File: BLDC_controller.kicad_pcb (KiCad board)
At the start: 4 copper layers, 100 x 100 mm, 1554 parts, among them P2 CONN_01X06, P3 CONN_01X05, P5 CONN_01X05, Q1 PSMN2R0-30YLD, Q2 PSMN2R0-30YLD, Q3 PSMN2R0-30YLD, Q4 PSMN2R0-30YLD, Q5 PSMN2R0-30YLD, Q6 PSMN2R0-30YLD

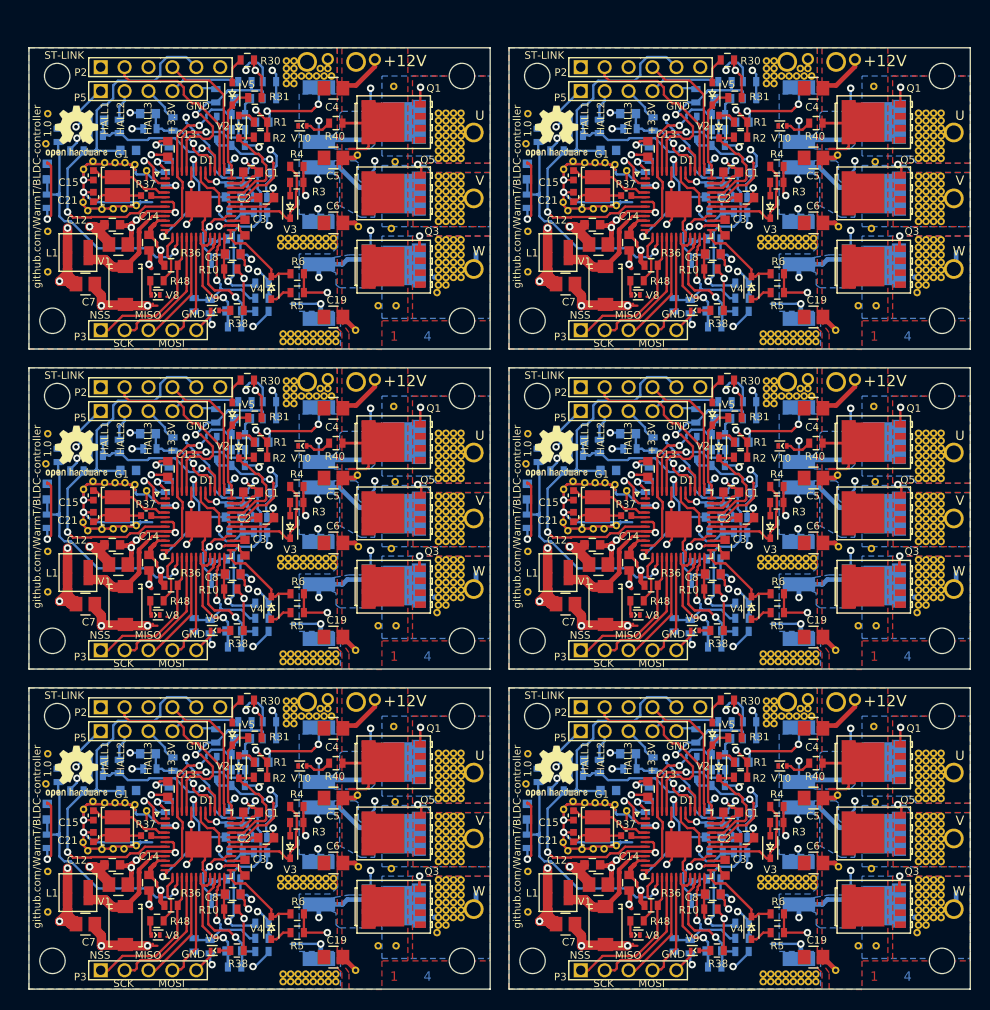
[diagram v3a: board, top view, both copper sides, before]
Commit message: QFN package improved
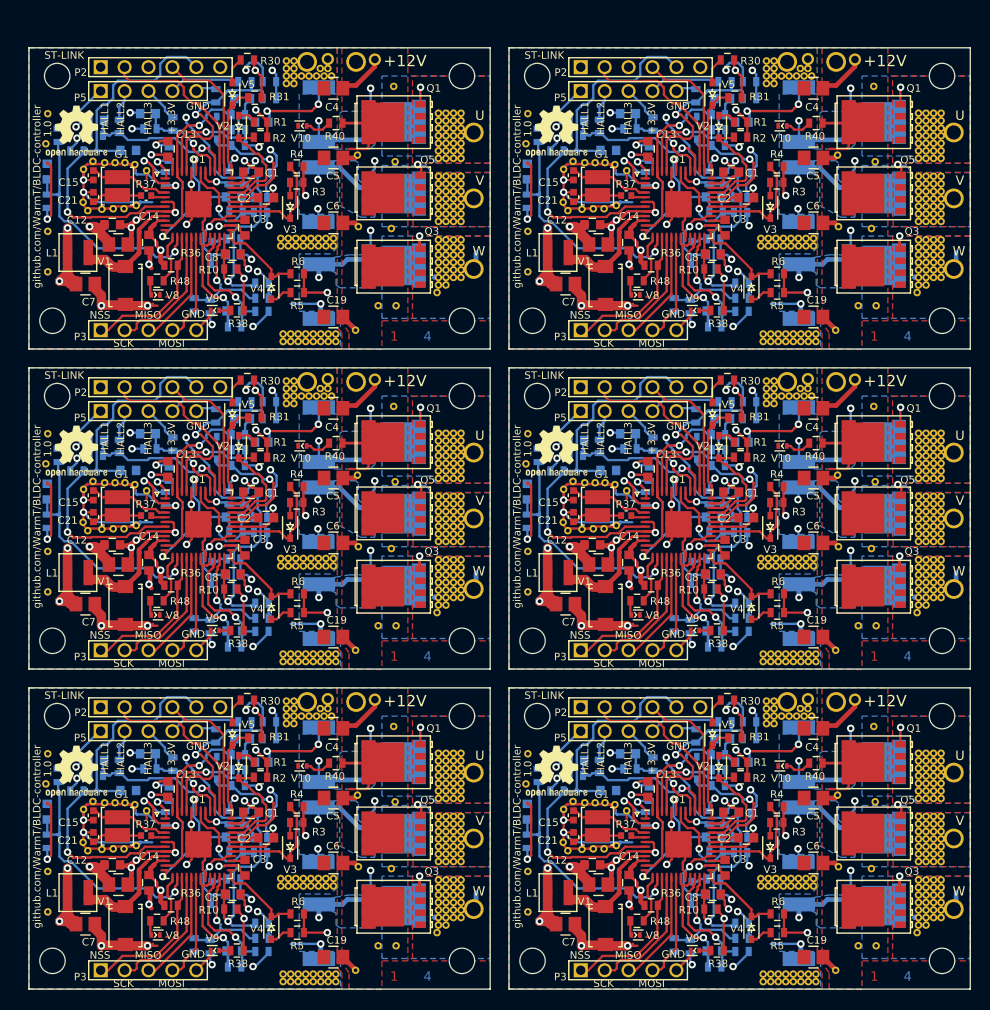
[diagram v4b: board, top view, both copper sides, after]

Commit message: Add Helsinki Hacklab logo
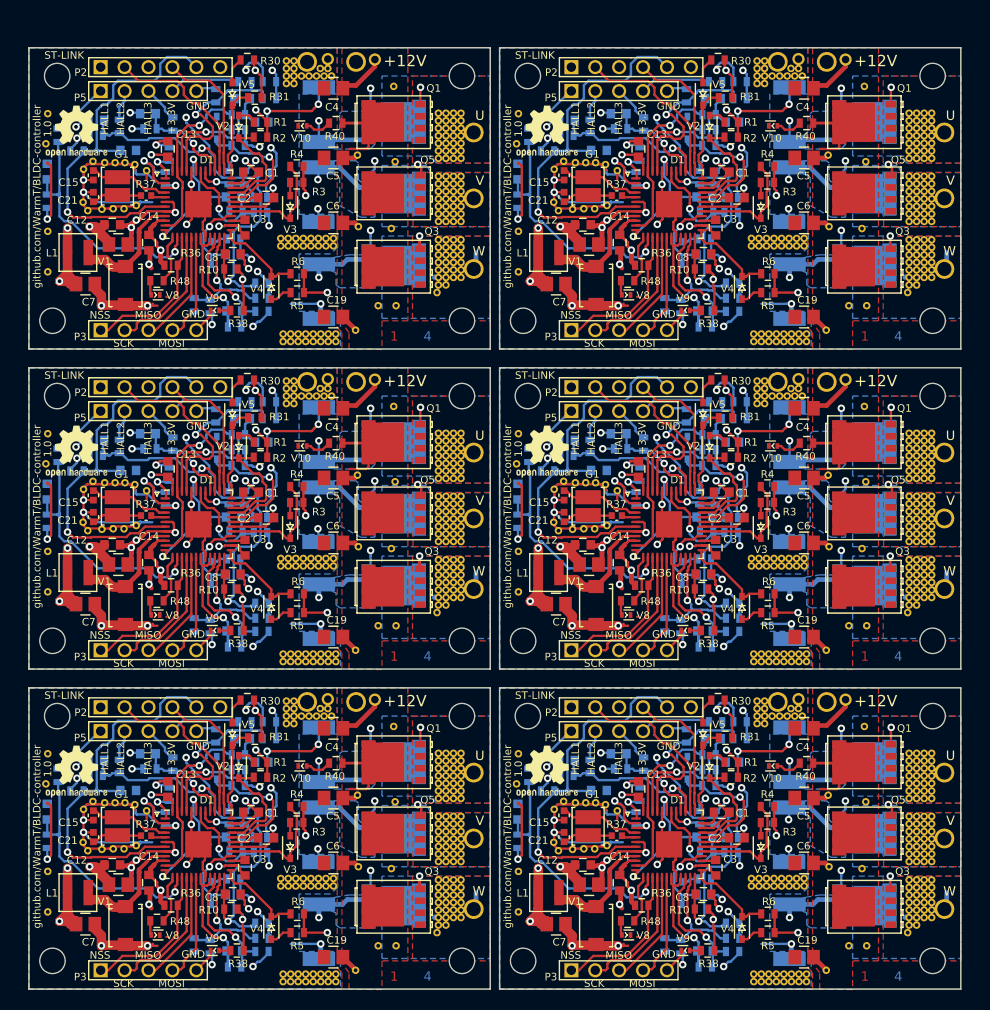
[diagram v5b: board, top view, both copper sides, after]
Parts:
- removed the C1 at (210.8, 162.2)
- removed the C1 at (210.8, 128.2)
- removed the C1 at (210.8, 94.2)
- removed the C10 at (209.0, 164.8)
- removed the C10 at (209.0, 130.8)
- removed the C10 at (209.0, 96.8)
- removed the C11 at (209.9, 154.4)
- removed the C11 at (209.9, 120.4)
- removed the C11 at (209.9, 86.4)
- removed the C12 at (196.1, 167.8)
- removed the C12 at (196.1, 133.8)
- removed the C12 at (196.1, 99.8)
- removed the C13 at (202.0, 159.8)
- removed the C13 at (202.0, 125.8)
- removed the C13 at (202.0, 91.8)
- removed the C14 at (200.0, 169.7)
- removed the C14 at (200.0, 135.7)
- removed the C14 at (200.0, 101.7)
- removed the C15 at (194.1, 162.6)
- removed the C15 at (194.1, 128.6)
- removed the C15 at (194.1, 94.5)
- removed the C16 at (197.8, 159.9)
- removed the C16 at (197.8, 125.9)
- removed the C16 at (197.8, 91.9)
- removed the C17 at (196.8, 169.9)
- removed the C17 at (196.8, 135.9)
- removed the C17 at (196.8, 101.9)
- removed the C19 at (219.6, 177.6)
- removed the C19 at (219.6, 143.6)
- removed the C19 at (219.6, 109.6)
- removed the C2 at (212.4, 164.9)
- removed the C2 at (212.4, 130.9)
- removed the C2 at (212.4, 96.9)
- removed the C21 at (194.1, 164.8)
- removed the C21 at (194.1, 130.8)
- removed the C21 at (194.1, 96.8)
- removed the C22 at (189.2, 162.2)
- removed the C22 at (189.2, 128.2)
- removed the C22 at (189.2, 94.2)
- removed the C23 at (194.4, 156.7)
- removed the C23 at (194.4, 122.7)
- removed the C23 at (194.4, 88.7)
- removed the C24 at (199.9, 156.0)
- removed the C24 at (199.9, 122.0)
- removed the C24 at (199.9, 88.0)
- removed the C3 at (210.2, 168.1)
- removed the C3 at (210.2, 134.1)
- removed the C3 at (210.2, 100.1)
- removed the C4 at (219.6, 153.3)
- removed the C4 at (219.6, 119.3)
- removed the C4 at (219.6, 85.3)
- removed the C5 at (219.6, 160.7)
- removed the C5 at (219.6, 126.7)
- removed the C5 at (219.6, 92.7)
- removed the C6 at (219.6, 167.6)
- removed the C6 at (219.6, 133.6)
- removed the C6 at (219.6, 99.6)
- removed the C7 at (193.2, 174.1)
- removed the C7 at (193.2, 140.1)
- removed the C7 at (193.2, 106.1)
- removed the C8 at (208.9, 170.9)
- removed the C8 at (208.9, 136.9)
- removed the C8 at (208.9, 102.9)
- removed the C9 at (209.1, 176.9)
- removed the C9 at (209.1, 142.9)
- removed the C9 at (209.1, 109.0)
- removed the D1 at (205.2, 165.6)
- removed the D1 at (205.2, 131.6)
- removed the D1 at (205.2, 97.6)
- removed the G1 at (196.7, 163.7)
- removed the G1 at (196.7, 129.7)
- removed the G1 at (196.7, 95.7)
- removed the L1 at (192.4, 170.8)
- removed the L1 at (192.4, 136.8)
- removed the L1 at (192.4, 102.8)
- removed the P2 at (201.2, 151.1)
- removed the P2 at (201.2, 117.1)
- removed the P2 at (201.2, 83.1)
- removed the P3 at (199.9, 179.0)
- removed the P3 at (199.9, 145.0)
- removed the P3 at (199.9, 111.0)
- removed the P5 at (199.9, 153.6)
- removed the P5 at (199.9, 119.6)
- removed the P5 at (199.9, 85.6)
- removed the Q1 at (226.0, 156.9)
- removed the Q1 at (226.0, 122.9)
- removed the Q1 at (226.0, 88.9)
- removed the Q2 at (226.0, 156.9)
- removed the Q2 at (226.0, 122.9)
- removed the Q2 at (226.0, 88.9)
- removed the Q3 at (226.0, 172.3)
- removed the Q3 at (226.0, 138.3)
- removed the Q3 at (226.0, 104.3)
- removed the Q4 at (226.0, 172.1)
- removed the Q4 at (226.0, 138.1)
- removed the Q4 at (226.0, 104.1)
- removed the Q5 at (226.0, 164.5)
- removed the Q5 at (226.0, 130.5)
- removed the Q5 at (226.0, 96.5)
- removed the Q6 at (226.0, 164.5)
- removed the Q6 at (226.0, 130.5)
- removed the Q6 at (226.0, 96.5)
- removed the R1 at (211.8, 156.9)
- removed the R1 at (211.8, 122.9)
- removed the R1 at (211.8, 88.9)
- removed the R10 at (208.7, 172.5)
- removed the R10 at (208.7, 138.5)
- removed the R10 at (208.7, 104.5)
- removed the R11 at (212.0, 174.0)
- removed the R11 at (212.0, 140.0)
- removed the R11 at (212.0, 106.0)
- removed the R12 at (212.2, 162.3)
- removed the R12 at (212.2, 128.3)
- removed the R12 at (212.2, 94.3)
- removed the R13 at (212.8, 152.6)
- removed the R13 at (212.8, 118.6)
- removed the R13 at (212.8, 84.6)
- removed the R14 at (212.0, 177.0)
- removed the R14 at (212.0, 143.0)
- removed the R14 at (212.0, 109.0)
- removed the R15 at (212.1, 156.9)
- removed the R15 at (212.1, 122.9)
- removed the R15 at (212.1, 88.9)
- removed the R16 at (211.8, 166.5)
- removed the R16 at (211.8, 132.5)
- removed the R16 at (211.8, 98.5)
- removed the R17 at (212.0, 175.6)
- removed the R17 at (212.0, 141.6)
- removed the R17 at (212.0, 107.6)
- removed the R18 at (211.8, 164.9)
- removed the R18 at (211.8, 130.9)
- removed the R18 at (211.8, 96.9)
- removed the R19 at (212.8, 154.4)
- removed the R19 at (212.8, 120.4)
- removed the R19 at (212.8, 86.4)
- removed the R2 at (211.8, 158.5)
- removed the R2 at (211.8, 124.5)
- removed the R2 at (211.8, 90.5)
- removed the R20 at (206.5, 176.5)
- removed the R20 at (206.5, 142.5)
- removed the R20 at (206.5, 108.5)
- removed the R21 at (210.2, 162.8)
- removed the R21 at (210.2, 128.8)
- removed the R21 at (210.2, 94.8)
- removed the R22 at (210.2, 152.6)
- removed the R22 at (210.2, 118.6)
- removed the R22 at (210.2, 84.6)
- removed the R23 at (204.8, 176.3)
- removed the R23 at (204.8, 142.3)
- removed the R23 at (204.8, 108.3)
- removed the R24 at (208.5, 162.8)
- removed the R24 at (208.5, 128.8)
- removed the R24 at (208.5, 94.8)
- removed the R25 at (207.1, 154.1)
- removed the R25 at (207.1, 120.1)
- removed the R25 at (207.1, 86.1)
- removed the R26 at (209.1, 178.7)
- removed the R26 at (209.1, 144.7)
- removed the R26 at (209.1, 110.7)
- removed the R27 at (209.2, 166.4)
- removed the R27 at (209.2, 132.4)
- removed the R27 at (209.2, 98.4)
- removed the R28 at (209.5, 156.1)
- removed the R28 at (209.5, 122.1)
- removed the R28 at (209.5, 88.1)
- removed the R29 at (202.2, 160.3)
- removed the R29 at (202.2, 126.3)
- removed the R29 at (202.2, 92.3)
- removed the R3 at (215.7, 163.3)
- removed the R3 at (215.7, 129.3)
- removed the R3 at (215.7, 95.3)
- removed the R30 at (210.4, 150.3)
- removed the R30 at (210.4, 116.3)
- removed the R30 at (210.4, 82.3)
- removed the R31 at (211.2, 154.3)
- removed the R31 at (211.2, 120.3)
- removed the R31 at (211.2, 86.3)
- removed the R32 at (209.5, 157.7)
- removed the R32 at (209.5, 123.7)
- removed the R32 at (209.5, 89.7)
- removed the R33 at (209.5, 159.4)
- removed the R33 at (209.5, 125.4)
- removed the R33 at (209.5, 91.4)
- removed the R34 at (209.0, 169.3)
- removed the R34 at (209.0, 135.3)
- removed the R34 at (209.0, 101.3)
- removed the R35 at (209.0, 171.0)
- removed the R35 at (209.0, 137.0)
- removed the R35 at (209.0, 103.0)
- removed the R36 at (202.3, 172.1)
- removed the R36 at (202.3, 138.1)
- removed the R36 at (202.3, 104.1)
- removed the R37 at (199.7, 164.7)
- removed the R37 at (199.7, 130.7)
- removed the R37 at (199.7, 96.7)
- removed the R38 at (209.3, 176.9)
- removed the R38 at (209.3, 142.9)
- removed the R38 at (209.3, 108.9)
- removed the R39 at (192.3, 159.9)
- removed the R39 at (192.3, 126.0)
- removed the R39 at (192.3, 92.0)
- removed the R4 at (215.7, 161.6)
- removed the R4 at (215.7, 127.6)
- removed the R4 at (215.7, 93.6)
- removed the R40 at (219.8, 157.0)
- removed the R40 at (219.8, 123.0)
- removed the R40 at (219.8, 89.0)
- removed the R41 at (190.3, 158.3)
- removed the R41 at (190.3, 124.3)
- removed the R41 at (190.3, 90.3)
- removed the R42 at (196.8, 157.3)
- removed the R42 at (196.8, 123.3)
- removed the R42 at (196.8, 89.3)
- removed the R43 at (202.6, 157.1)
- removed the R43 at (202.6, 123.1)
- removed the R43 at (202.6, 89.1)
- removed the R44 at (189.2, 165.3)
- removed the R44 at (189.2, 131.3)
- removed the R44 at (189.2, 97.3)
- removed the R45 at (194.4, 158.3)
- removed the R45 at (194.4, 124.3)
- removed the R45 at (194.4, 90.3)
- removed the R46 at (200.1, 157.6)
- removed the R46 at (200.1, 123.6)
- removed the R46 at (200.1, 89.6)
- removed the R47 at (201.8, 162.9)
- removed the R47 at (201.8, 128.9)
- removed the R47 at (201.8, 94.9)
- removed the R48 at (200.8, 173.8)
- removed the R48 at (200.8, 139.8)
- removed the R48 at (200.8, 105.8)
- removed the R5 at (215.8, 175.0)
- removed the R5 at (215.8, 141.0)
- removed the R5 at (215.8, 107.0)
- removed the R6 at (215.8, 173.0)
- removed the R6 at (215.8, 139.0)
- removed the R6 at (215.8, 105.0)
- removed the R7 at (218.1, 174.9)
- removed the R7 at (218.1, 140.9)
- removed the R7 at (218.1, 106.9)
- removed the R8 at (218.0, 164.6)
- removed the R8 at (218.0, 130.6)
- removed the R8 at (218.0, 96.6)
- removed the R9 at (218.1, 156.1)
- removed the R9 at (218.1, 122.1)
- removed the R9 at (218.1, 88.1)
- removed the REF** at (190.2, 152.0)
- removed the REF** at (189.1, 91.2)
- removed the REF** at (230.8, 103.8)
- removed the REF** at (234.5, 172.5)
- removed the REF** at (234.5, 138.5)
- removed the REF** at (234.5, 104.5)
- removed the REF** at (231.6, 174.2)
- removed the REF** at (231.6, 140.2)
- removed the REF** at (189.2, 156.0)
- removed the REF** at (231.6, 106.2)
- removed the REF** at (233.2, 173.4)
- removed the REF** at (233.2, 139.4)
- removed the REF** at (233.2, 105.4)
- removed the REF** at (231.6, 171.8)
- removed the REF** at (231.6, 137.8)
- removed the REF** at (231.6, 103.8)
- removed the REF** at (232.3, 172.6)
- removed the REF** at (232.3, 138.6)
- removed the REF** at (232.3, 104.6)
- removed the REF** at (232.3, 171.8)
- removed the REF** at (232.3, 137.8)
- removed the REF** at (189.2, 122.0)
- removed the REF** at (232.3, 103.8)
- removed the REF** at (233.2, 172.6)
- removed the REF** at (233.2, 138.6)
- removed the REF** at (233.2, 104.6)
- removed the REF** at (231.6, 172.6)
- removed the REF** at (231.6, 138.6)
- removed the REF** at (231.6, 104.6)
- removed the REF** at (233.2, 171.8)
- removed the REF** at (233.2, 137.8)
- removed the REF** at (233.2, 103.8)
- removed the REF** at (230.8, 173.4)
- removed the REF** at (230.8, 139.4)
- removed the REF** at (189.2, 88.0)
- removed the REF** at (230.8, 105.4)
- removed the REF** at (230.8, 174.2)
- removed the REF** at (230.8, 140.2)
- removed the REF** at (230.8, 106.2)
- removed the REF** at (230.8, 172.6)
- removed the REF** at (230.8, 138.6)
- removed the REF** at (193.5, 166.3)
- removed the REF** at (230.8, 104.6)
- removed the REF** at (230.6, 175.0)
- removed the REF** at (230.6, 141.0)
- removed the REF** at (230.6, 107.0)
- removed the REF** at (230.8, 169.4)
- removed the REF** at (230.8, 135.4)
- removed the REF** at (230.8, 101.4)
- removed the REF** at (230.8, 171.0)
- removed the REF** at (230.8, 137.0)
- removed the REF** at (230.8, 103.0)
- removed the REF** at (231.6, 170.2)
- removed the REF** at (231.6, 136.2)
- removed the REF** at (193.5, 132.3)
- removed the REF** at (231.6, 102.2)
- removed the REF** at (231.6, 171.0)
- removed the REF** at (231.6, 137.0)
- removed the REF** at (231.6, 103.0)
- removed the REF** at (231.6, 169.4)
- removed the REF** at (231.6, 135.4)
- removed the REF** at (231.6, 101.4)
- removed the REF** at (230.8, 170.2)
- removed the REF** at (230.8, 136.2)
- removed the REF** at (230.8, 102.2)
- removed the REF** at (232.3, 169.4)
- removed the REF** at (232.3, 135.4)
- removed the REF** at (193.5, 98.3)
- removed the REF** at (232.3, 101.4)
- removed the REF** at (233.2, 171.0)
- removed the REF** at (233.2, 137.0)
- removed the REF** at (233.2, 103.0)
- removed the REF** at (233.2, 169.4)
- removed the REF** at (233.2, 135.4)
- removed the REF** at (193.1, 161.9)
- removed the REF** at (233.2, 101.4)
- removed the REF** at (232.3, 171.0)
- removed the REF** at (232.3, 137.0)
- removed the REF** at (232.3, 103.0)
- removed the REF** at (232.3, 170.2)
- removed the REF** at (232.3, 136.2)
- removed the REF** at (232.3, 102.2)
- removed the REF** at (233.2, 170.2)
- removed the REF** at (233.2, 136.2)
- removed the REF** at (233.2, 102.2)
- removed the REF** at (232.3, 165.8)
- removed the REF** at (232.3, 131.8)
- removed the REF** at (193.1, 127.9)
- removed the REF** at (232.3, 97.8)
- removed the REF** at (233.2, 167.4)
- removed the REF** at (233.2, 133.4)
- removed the REF** at (233.2, 99.5)
- removed the REF** at (233.2, 166.7)
- removed the REF** at (233.2, 132.7)
- removed the REF** at (233.2, 98.7)
- removed the REF** at (232.3, 166.7)
- removed the REF** at (232.3, 132.7)
- removed the REF** at (232.3, 98.7)
- removed the REF** at (232.3, 167.4)
- removed the REF** at (232.3, 133.4)
- removed the REF** at (193.1, 93.9)
- removed the REF** at (232.3, 99.5)
- removed the REF** at (233.2, 165.8)
- removed the REF** at (233.2, 131.8)
- removed the REF** at (233.2, 97.8)
- removed the REF** at (230.8, 165.8)
- removed the REF** at (230.8, 131.8)
- removed the REF** at (193.0, 165.4)
- removed the REF** at (230.8, 97.8)
- removed the REF** at (231.6, 167.4)
- removed the REF** at (231.6, 133.4)
- removed the REF** at (231.6, 99.5)
- removed the REF** at (230.8, 167.4)
- removed the REF** at (230.8, 133.4)
- removed the REF** at (230.8, 99.5)
- removed the REF** at (231.6, 166.7)
- removed the REF** at (231.6, 132.7)
- removed the REF** at (231.6, 98.7)
- removed the REF** at (230.8, 166.7)
- removed the REF** at (230.8, 132.7)
- removed the REF** at (193.0, 131.4)
- removed the REF** at (230.8, 98.7)
- removed the REF** at (231.6, 165.8)
- removed the REF** at (231.6, 131.8)
- removed the REF** at (231.6, 97.8)
- removed the REF** at (233.2, 157.6)
- removed the REF** at (233.2, 123.5)
- removed the REF** at (233.2, 89.5)
- removed the REF** at (233.2, 156.8)
- removed the REF** at (233.2, 122.8)
- removed the REF** at (233.2, 88.8)
- removed the REF** at (230.8, 155.9)
- removed the REF** at (230.8, 122.0)
- removed the REF** at (190.2, 118.0)
- removed the REF** at (193.0, 97.4)
- removed the REF** at (230.8, 88.0)
- removed the REF** at (230.8, 156.8)
- removed the REF** at (230.8, 122.8)
- removed the REF** at (230.8, 88.8)
- removed the REF** at (231.6, 156.8)
- removed the REF** at (231.6, 122.8)
- removed the REF** at (195.3, 161.2)
- removed the REF** at (231.6, 88.8)
- removed the REF** at (232.3, 156.8)
- removed the REF** at (232.3, 122.8)
- removed the REF** at (232.3, 88.8)
- removed the REF** at (233.2, 152.0)
- removed the REF** at (233.2, 118.0)
- removed the REF** at (233.2, 84.0)
- removed the REF** at (233.2, 155.9)
- removed the REF** at (233.2, 122.0)
- removed the REF** at (233.2, 88.0)
- removed the REF** at (231.6, 155.9)
- removed the REF** at (231.6, 122.0)
- removed the REF** at (195.3, 127.2)
- removed the REF** at (231.6, 88.0)
- removed the REF** at (232.3, 155.9)
- removed the REF** at (232.3, 122.0)
- removed the REF** at (232.3, 88.0)
- removed the REF** at (232.3, 158.3)
- removed the REF** at (232.3, 124.3)
- removed the REF** at (232.3, 90.3)
- removed the REF** at (230.8, 157.6)
- removed the REF** at (230.8, 123.5)
- removed the REF** at (230.8, 89.5)
- removed the REF** at (231.6, 158.3)
- removed the REF** at (231.6, 124.3)
- removed the REF** at (195.3, 93.2)
- removed the REF** at (231.6, 90.3)
- removed the REF** at (231.6, 157.6)
- removed the REF** at (231.6, 123.5)
- removed the REF** at (231.6, 89.5)
- removed the REF** at (230.8, 158.3)
- removed the REF** at (230.8, 124.3)
- removed the REF** at (198.5, 161.4)
- removed the REF** at (230.8, 90.3)
- removed the REF** at (232.3, 157.6)
- removed the REF** at (232.3, 123.5)
- removed the REF** at (232.3, 89.5)
- removed the REF** at (230.8, 159.2)
- removed the REF** at (230.8, 125.2)
- removed the REF** at (230.8, 91.2)
- removed the REF** at (231.6, 159.2)
- removed the REF** at (231.6, 125.2)
- removed the REF** at (231.6, 91.2)
- removed the REF** at (232.3, 159.2)
- removed the REF** at (232.3, 125.2)
- removed the REF** at (198.5, 127.4)
- removed the REF** at (232.3, 91.2)
- removed the REF** at (231.6, 159.9)
- removed the REF** at (231.6, 126.0)
- removed the REF** at (231.6, 92.0)
- removed the REF** at (230.8, 159.9)
- removed the REF** at (230.8, 126.0)
- removed the REF** at (230.8, 92.0)
- removed the REF** at (233.2, 158.3)
- removed the REF** at (233.2, 124.3)
- removed the REF** at (233.2, 90.3)
- removed the REF** at (234.5, 158.0)
- removed the REF** at (234.5, 124.0)
- removed the REF** at (198.5, 93.4)
- removed the REF** at (234.5, 90.0)
- removed the REF** at (232.3, 159.9)
- removed the REF** at (232.3, 126.0)
- removed the REF** at (232.3, 92.0)
- removed the REF** at (232.3, 160.8)
- removed the REF** at (232.3, 126.8)
- removed the REF** at (197.4, 161.2)
- removed the REF** at (232.3, 92.8)
- removed the REF** at (233.2, 159.9)
- removed the REF** at (233.2, 126.0)
- removed the REF** at (233.2, 92.0)
- removed the REF** at (233.2, 160.8)
- removed the REF** at (233.2, 126.8)
- removed the REF** at (233.2, 92.8)
- removed the REF** at (233.2, 159.2)
- removed the REF** at (233.2, 125.2)
- removed the REF** at (233.2, 91.2)
- removed the REF** at (230.8, 162.7)
- removed the REF** at (230.8, 128.7)
- removed the REF** at (197.4, 127.2)
- removed the REF** at (230.8, 94.7)
- removed the REF** at (232.3, 162.7)
- removed the REF** at (232.3, 128.7)
- removed the REF** at (232.3, 94.7)
- removed the REF** at (231.6, 162.7)
- removed the REF** at (231.6, 128.7)
- removed the REF** at (231.6, 94.7)
- removed the REF** at (233.2, 162.7)
- removed the REF** at (233.2, 128.7)
- removed the REF** at (233.2, 94.7)
- removed the REF** at (230.8, 160.8)
- removed the REF** at (230.8, 126.8)
- removed the REF** at (197.4, 93.2)
- removed the REF** at (230.8, 92.8)
- removed the REF** at (231.6, 160.8)
- removed the REF** at (231.6, 126.8)
- removed the REF** at (231.6, 92.8)
- removed the REF** at (232.3, 165.1)
- removed the REF** at (232.3, 131.1)
- removed the REF** at (194.1, 161.1)
- removed the REF** at (232.3, 97.0)
- removed the REF** at (233.2, 163.4)
- removed the REF** at (233.2, 129.4)
- removed the REF** at (233.2, 95.5)
- removed the REF** at (232.3, 163.4)
- removed the REF** at (232.3, 129.4)
- removed the REF** at (232.3, 95.5)
- removed the REF** at (233.2, 164.2)
- removed the REF** at (233.2, 130.2)
- removed the REF** at (233.2, 96.2)
- removed the REF** at (233.2, 165.1)
- removed the REF** at (233.2, 131.1)
- removed the REF** at (194.1, 127.1)
- removed the REF** at (233.2, 97.0)
- removed the REF** at (234.5, 165.0)
- removed the REF** at (234.5, 131.0)
- removed the REF** at (234.5, 97.0)
- removed the REF** at (232.3, 164.2)
- removed the REF** at (232.3, 130.2)
- removed the REF** at (232.3, 96.2)
- removed the REF** at (230.8, 163.4)
- removed the REF** at (230.8, 129.4)
- removed the REF** at (230.8, 95.5)
- removed the REF** at (231.6, 164.2)
- removed the REF** at (231.6, 130.2)
- removed the REF** at (190.2, 84.0)
- removed the REF** at (194.1, 93.1)
- removed the REF** at (231.6, 96.2)
- removed the REF** at (230.8, 165.1)
- removed the REF** at (230.8, 131.1)
- removed the REF** at (230.8, 97.0)
- removed the REF** at (231.6, 163.4)
- removed the REF** at (231.6, 129.4)
- removed the REF** at (196.4, 161.2)
- removed the REF** at (231.6, 95.5)
- removed the REF** at (231.6, 165.1)
- removed the REF** at (231.6, 131.1)
- removed the REF** at (231.6, 97.0)
- removed the REF** at (230.8, 164.2)
- removed the REF** at (230.8, 130.2)
- removed the REF** at (230.8, 96.2)
- removed the REF** at (198.7, 165.8)
- removed the REF** at (198.7, 131.8)
- removed the REF** at (198.7, 97.8)
- removed the REF** at (199.8, 162.1)
- removed the REF** at (199.8, 128.1)
- removed the REF** at (196.4, 127.2)
- removed the REF** at (199.8, 94.1)
- removed the REF** at (189.8, 178.0)
- removed the REF** at (189.8, 144.0)
- removed the REF** at (189.8, 110.0)
- removed the REF** at (189.2, 168.5)
- removed the REF** at (189.2, 134.5)
- removed the REF** at (189.2, 100.5)
- removed the REF** at (189.2, 172.8)
- removed the REF** at (189.2, 138.8)
- removed the REF** at (189.2, 104.8)
- removed the REF** at (195.0, 166.2)
- removed the REF** at (195.0, 132.2)
- removed the REF** at (196.4, 93.2)
- removed the REF** at (195.0, 98.2)
- removed the REF** at (197.3, 166.1)
- removed the REF** at (197.3, 132.1)
- removed the REF** at (197.3, 98.1)
- removed the REF** at (196.2, 166.1)
- removed the REF** at (196.2, 132.1)
- removed the REF** at (224.3, 176.4)
- removed the REF** at (196.2, 98.1)
- removed the REF** at (219.1, 179.4)
- removed the REF** at (219.1, 145.4)
- removed the REF** at (219.1, 111.4)
- removed the REF** at (218.2, 179.4)
- removed the REF** at (218.2, 145.4)
- removed the REF** at (218.2, 111.4)
- removed the REF** at (219.8, 179.4)
- removed the REF** at (219.8, 145.4)
- removed the REF** at (219.8, 111.4)
- removed the REF** at (214.2, 179.4)
- removed the REF** at (214.2, 145.4)
- removed the REF** at (224.3, 142.4)
- removed the REF** at (214.2, 111.4)
- removed the REF** at (216.7, 179.4)
- removed the REF** at (216.7, 145.4)
- removed the REF** at (216.7, 111.4)
- removed the REF** at (214.2, 180.2)
- removed the REF** at (214.2, 146.2)
- removed the REF** at (214.2, 112.2)
- removed the REF** at (215.1, 179.4)
- removed the REF** at (215.1, 145.4)
- removed the REF** at (215.1, 111.4)
- removed the REF** at (215.1, 180.2)
- removed the REF** at (215.1, 146.2)
- removed the REF** at (189.1, 159.2)
- removed the REF** at (224.3, 108.4)
- removed the REF** at (215.1, 112.2)
- removed the REF** at (215.8, 180.2)
- removed the REF** at (215.8, 146.2)
- removed the REF** at (215.8, 112.2)
- removed the REF** at (216.7, 180.2)
- removed the REF** at (216.7, 146.2)
- removed the REF** at (226.2, 176.4)
- removed the REF** at (216.7, 112.2)
- removed the REF** at (215.8, 179.4)
- removed the REF** at (215.8, 145.4)
- removed the REF** at (215.8, 111.4)
- removed the REF** at (214.0, 169.2)
- removed the REF** at (214.0, 135.2)
- removed the REF** at (214.0, 101.2)
- removed the REF** at (214.8, 169.2)
- removed the REF** at (214.8, 135.2)
- removed the REF** at (214.8, 101.2)
- removed the REF** at (215.6, 169.2)
- removed the REF** at (215.6, 135.2)
- removed the REF** at (226.2, 142.4)
- removed the REF** at (215.6, 101.2)
- removed the REF** at (216.4, 169.2)
- removed the REF** at (216.4, 135.2)
- removed the REF** at (216.4, 101.2)
- removed the REF** at (214.0, 170.1)
- removed the REF** at (214.0, 136.1)
- removed the REF** at (214.0, 102.0)
- removed the REF** at (217.4, 179.4)
- removed the REF** at (217.4, 145.4)
- removed the REF** at (217.4, 111.4)
- removed the REF** at (217.4, 180.2)
- removed the REF** at (217.4, 146.2)
- removed the REF** at (226.2, 108.4)
- removed the REF** at (217.4, 112.2)
- removed the REF** at (218.2, 180.2)
- removed the REF** at (218.2, 146.2)
- removed the REF** at (218.2, 112.2)
- removed the REF** at (219.1, 180.2)
- removed the REF** at (219.1, 146.2)
- removed the REF** at (222.2, 168.0)
- removed the REF** at (219.1, 112.2)
- removed the REF** at (219.8, 180.2)
- removed the REF** at (219.8, 146.2)
- removed the REF** at (219.8, 112.2)
- removed the REF** at (217.2, 169.2)
- removed the REF** at (217.2, 135.2)
- removed the REF** at (217.2, 101.2)
- removed the REF** at (219.6, 169.2)
- removed the REF** at (219.6, 135.2)
- removed the REF** at (219.6, 101.2)
- removed the REF** at (218.8, 170.1)
- removed the REF** at (218.8, 136.1)
- removed the REF** at (222.2, 134.0)
- removed the REF** at (218.8, 102.0)
- removed the REF** at (219.6, 170.1)
- removed the REF** at (219.6, 136.1)
- removed the REF** at (219.6, 102.0)
- removed the REF** at (218.0, 170.1)
- removed the REF** at (218.0, 136.1)
- removed the REF** at (218.0, 102.0)
- removed the REF** at (218.8, 169.2)
- removed the REF** at (218.8, 135.2)
- removed the REF** at (218.8, 101.2)
- removed the REF** at (218.0, 169.2)
- removed the REF** at (218.0, 135.2)
- removed the REF** at (222.2, 100.0)
- removed the REF** at (218.0, 101.2)
- removed the REF** at (217.2, 170.1)
- removed the REF** at (217.2, 136.1)
- removed the REF** at (217.2, 102.0)
- removed the REF** at (215.6, 170.1)
- removed the REF** at (215.6, 136.1)
- removed the REF** at (221.9, 179.0)
- removed the REF** at (215.6, 102.0)
- removed the REF** at (214.8, 170.1)
- removed the REF** at (214.8, 136.1)
- removed the REF** at (214.8, 102.0)
- removed the REF** at (216.4, 170.1)
- removed the REF** at (216.4, 136.1)
- removed the REF** at (216.4, 102.0)
- removed the REF** at (218.2, 151.2)
- removed the REF** at (218.2, 117.2)
- removed the REF** at (218.2, 83.2)
- removed the REF** at (216.2, 152.0)
- removed the REF** at (216.2, 118.0)
- removed the REF** at (221.9, 145.0)
- removed the REF** at (216.2, 84.0)
- removed the REF** at (217.0, 152.0)
- removed the REF** at (217.0, 118.0)
- removed the REF** at (217.0, 84.0)
- removed the REF** at (216.8, 150.5)
- removed the REF** at (216.8, 116.5)
- removed the REF** at (216.8, 82.5)
- removed the REF** at (218.6, 152.0)
- removed the REF** at (218.6, 118.0)
- removed the REF** at (218.6, 84.0)
- removed the REF** at (217.8, 152.0)
- removed the REF** at (217.8, 118.0)
- removed the REF** at (221.9, 111.0)
- removed the REF** at (217.8, 84.0)
- removed the REF** at (226.2, 161.1)
- removed the REF** at (226.2, 127.1)
- removed the REF** at (226.2, 93.1)
- removed the REF** at (222.2, 160.4)
- removed the REF** at (222.2, 126.4)
- removed the REF** at (225.8, 168.2)
- removed the REF** at (222.2, 92.4)
- removed the REF** at (215.4, 152.8)
- removed the REF** at (215.4, 118.8)
- removed the REF** at (215.4, 84.8)
- removed the REF** at (214.6, 152.8)
- removed the REF** at (214.6, 118.8)
- removed the REF** at (214.6, 84.8)
- removed the REF** at (214.6, 152.0)
- removed the REF** at (214.6, 118.0)
- removed the REF** at (214.6, 84.0)
- removed the REF** at (215.4, 151.2)
- removed the REF** at (215.4, 117.2)
- removed the REF** at (225.8, 134.2)
- removed the REF** at (215.4, 83.2)
- removed the REF** at (214.6, 151.2)
- removed the REF** at (214.6, 117.2)
- removed the REF** at (214.6, 83.2)
- removed the REF** at (215.4, 150.4)
- removed the REF** at (215.4, 116.4)
- removed the REF** at (215.4, 82.4)
- removed the REF** at (215.4, 152.0)
- removed the REF** at (215.4, 118.0)
- removed the REF** at (215.4, 84.0)
- removed the REF** at (214.6, 150.4)
- removed the REF** at (214.6, 116.4)
- removed the REF** at (189.1, 125.2)
- removed the REF** at (225.8, 100.2)
- removed the REF** at (214.6, 82.4)
- removed the REF** at (219.4, 152.0)
- removed the REF** at (219.4, 118.0)
- removed the REF** at (219.4, 84.0)
- removed the REF** at (226.0, 153.1)
- removed the REF** at (226.0, 119.1)
- removed the REF** at (233.2, 178.0)
- removed the REF** at (226.0, 85.1)
- removed the REF** at (224.0, 150.2)
- removed the REF** at (224.0, 116.2)
- removed the REF** at (224.0, 82.2)
- removed the REF** at (219.0, 150.2)
- removed the REF** at (219.0, 116.2)
- removed the REF** at (219.0, 82.2)
- removed the REF** at (219.0, 151.2)
- removed the REF** at (219.0, 117.2)
- removed the REF** at (219.0, 83.2)
- removed the REF** at (222.0, 150.5)
- removed the REF** at (222.0, 116.5)
- removed the REF** at (233.2, 144.0)
- removed the REF** at (222.0, 82.5)
- removed the REF** at (233.2, 110.0)
- removed the REF** at (231.6, 173.4)
- removed the REF** at (231.6, 139.4)
- removed the REF** at (231.6, 105.4)
- removed the REF** at (232.3, 173.4)
- removed the REF** at (232.3, 139.4)
- removed the REF** at (232.3, 105.4)
- removed the REF** at (230.8, 171.8)
- removed the REF** at (230.8, 137.8)
- removed the REF*** at (192.3, 157.9)
- removed the REF*** at (192.3, 123.9)
- removed the REF*** at (192.3, 89.9)
- removed the V1 at (197.5, 174.2)
- removed the V1 at (197.5, 140.2)
- removed the V1 at (197.5, 106.2)
- removed the V10 at (216.3, 157.3)
- removed the V10 at (216.3, 123.3)
- removed the V10 at (216.3, 89.3)
- removed the V2 at (209.6, 157.4)
- removed the V2 at (209.6, 123.4)
- removed the V2 at (209.6, 89.4)
- removed the V3 at (215.0, 165.9)
- removed the V3 at (215.0, 131.9)
- removed the V3 at (215.0, 97.9)
- removed the V4 at (213.0, 174.5)
- removed the V4 at (213.0, 140.5)
- removed the V4 at (213.0, 106.5)
- removed the V5 at (208.8, 153.9)
- removed the V5 at (208.8, 119.9)
- removed the V5 at (208.8, 85.9)
- removed the V6 at (207.2, 157.5)
- removed the V6 at (207.2, 123.5)
- removed the V6 at (207.2, 89.5)
- removed the V7 at (206.6, 170.8)
- removed the V7 at (206.6, 136.8)
- removed the V7 at (206.6, 102.8)
- removed the V8 at (200.7, 175.2)
- removed the V8 at (200.7, 141.2)
- removed the V8 at (200.7, 107.2)
- removed the V9 at (207.0, 176.9)
- removed the V9 at (207.0, 142.9)
- removed the V9 at (207.0, 108.9)
- added C1: 100n, project_footprints:C_0603, F.Cu at (209.8, 162.2)
- added C1: 100n, project_footprints:C_0603, F.Cu at (209.8, 128.2)
- added C1: 100n, project_footprints:C_0603, F.Cu at (209.8, 94.2)
- added C10: 100p, project_footprints:C_0603, B.Cu at (208.0, 164.8)
- added C10: 100p, project_footprints:C_0603, B.Cu at (208.0, 130.8)
- added C10: 100p, project_footprints:C_0603, B.Cu at (208.0, 96.8)
- added C11: 100p, project_footprints:C_0603, B.Cu at (208.9, 154.4)
- added C11: 100p, project_footprints:C_0603, B.Cu at (208.9, 120.4)
- added C11: 100p, project_footprints:C_0603, B.Cu at (208.9, 86.4)
- added C12: 100n, project_footprints:C_0603, F.Cu at (195.1, 167.8)
- added C12: 100n, project_footprints:C_0603, F.Cu at (195.1, 133.8)
- added C12: 100n, project_footprints:C_0603, F.Cu at (195.1, 99.8)
- added C13: 100n, project_footprints:C_0603, F.Cu at (201.0, 159.8)
- added C13: 100n, project_footprints:C_0603, F.Cu at (201.0, 125.8)
- added C13: 100n, project_footprints:C_0603, F.Cu at (201.0, 91.8)
- added C14: 100n, project_footprints:C_0603, F.Cu at (199.0, 169.7)
- added C14: 100n, project_footprints:C_0603, F.Cu at (199.0, 135.7)
- added C14: 100n, project_footprints:C_0603, F.Cu at (199.0, 101.7)
- added C15: 10p, project_footprints:C_0402, F.Cu at (193.1, 162.6)
- added C15: 10p, project_footprints:C_0402, F.Cu at (193.1, 128.6)
- added C15: 10p, project_footprints:C_0402, F.Cu at (193.1, 94.5)
- added C16: 3n3, project_footprints:C_0603, B.Cu at (196.8, 159.9)
- added C16: 3n3, project_footprints:C_0603, B.Cu at (196.8, 125.9)
- added C16: 3n3, project_footprints:C_0603, B.Cu at (196.8, 91.9)
- added C17: 220n, project_footprints:C_0805, F.Cu at (195.8, 169.9)
- added C17: 220n, project_footprints:C_0805, F.Cu at (195.8, 135.9)
- added C17: 220n, project_footprints:C_0805, F.Cu at (195.8, 101.9)
- added C19: 220n, project_footprints:C_0805, F.Cu at (218.6, 177.6)
- added C19: 220n, project_footprints:C_0805, F.Cu at (218.6, 143.6)
- added C19: 220n, project_footprints:C_0805, F.Cu at (218.6, 109.6)
- added C2: 100n, project_footprints:C_0603, F.Cu at (211.4, 164.9)
- added C2: 100n, project_footprints:C_0603, F.Cu at (211.4, 130.9)
- added C2: 100n, project_footprints:C_0603, F.Cu at (211.4, 96.9)
- added C21: 10p, project_footprints:C_0402, F.Cu at (193.1, 164.8)
- added C21: 10p, project_footprints:C_0402, F.Cu at (193.1, 130.8)
- added C21: 10p, project_footprints:C_0402, F.Cu at (193.1, 96.8)
- added C22: 10p, project_footprints:C_0603, B.Cu at (188.2, 162.2)
- added C22: 10p, project_footprints:C_0603, B.Cu at (188.2, 128.2)
- added C22: 10p, project_footprints:C_0603, B.Cu at (188.2, 94.2)
- added C23: 10p, project_footprints:C_0603, B.Cu at (193.4, 156.7)
- added C23: 10p, project_footprints:C_0603, B.Cu at (193.4, 122.7)
- added C23: 10p, project_footprints:C_0603, B.Cu at (193.4, 88.7)
- added C24: 10p, project_footprints:C_0603, B.Cu at (198.9, 156.0)
- added C24: 10p, project_footprints:C_0603, B.Cu at (198.9, 122.0)
- added C24: 10p, project_footprints:C_0603, B.Cu at (198.9, 88.0)
- added C3: 100n, project_footprints:C_0603, F.Cu at (209.2, 168.1)
- added C3: 100n, project_footprints:C_0603, F.Cu at (209.2, 134.1)
- added C3: 100n, project_footprints:C_0603, F.Cu at (209.2, 100.1)
- added C4: 220n, project_footprints:C_0805, F.Cu at (218.6, 153.3)
- added C4: 220n, project_footprints:C_0805, F.Cu at (218.6, 119.3)
- added C4: 220n, project_footprints:C_0805, F.Cu at (218.6, 85.3)
- added C5: 220n, project_footprints:C_0805, F.Cu at (218.6, 160.7)
- added C5: 220n, project_footprints:C_0805, F.Cu at (218.6, 126.7)
- added C5: 220n, project_footprints:C_0805, F.Cu at (218.6, 92.7)
- added C6: 220n, project_footprints:C_0805, F.Cu at (218.6, 167.6)
- added C6: 220n, project_footprints:C_0805, F.Cu at (218.6, 133.6)
- added C6: 220n, project_footprints:C_0805, F.Cu at (218.6, 99.6)
- added C7: 47u, project_footprints:C_0805, F.Cu at (192.2, 174.1)
- added C7: 47u, project_footprints:C_0805, F.Cu at (192.2, 140.1)
- added C7: 47u, project_footprints:C_0805, F.Cu at (192.2, 106.1)
- added C8: 1n0, project_footprints:C_0603, F.Cu at (207.9, 170.9)
- added C8: 1n0, project_footprints:C_0603, F.Cu at (207.9, 136.9)
- added C8: 1n0, project_footprints:C_0603, F.Cu at (207.9, 102.9)
- added C9: 100p, project_footprints:C_0603, B.Cu at (208.1, 176.9)
- added C9: 100p, project_footprints:C_0603, B.Cu at (208.1, 142.9)
- added C9: 100p, project_footprints:C_0603, B.Cu at (208.1, 109.0)
- added D1: STSPIN32F0, project_footprints:QFN-48-1EP_7x7mm_Pitch0.5mm, F.Cu at (204.2, 165.6)
- added D1: STSPIN32F0, project_footprints:QFN-48-1EP_7x7mm_Pitch0.5mm, F.Cu at (204.2, 131.6)
- added D1: STSPIN32F0, project_footprints:QFN-48-1EP_7x7mm_Pitch0.5mm, F.Cu at (204.2, 97.6)
- added G***: LOGO, graphics:Logo_Helsinki_Hacklab, B.Cu at (195.2, 171.3)
- added G***: LOGO, graphics:Logo_Helsinki_Hacklab, B.Cu at (145.2, 171.3)
- added G***: LOGO, graphics:Logo_Helsinki_Hacklab, B.Cu at (195.2, 137.3)
- added G***: LOGO, graphics:Logo_Helsinki_Hacklab, B.Cu at (145.2, 137.3)
- added G***: LOGO, graphics:Logo_Helsinki_Hacklab, B.Cu at (195.2, 103.3)
- added G***: LOGO, graphics:Logo_Helsinki_Hacklab, B.Cu at (145.2, 103.3)
- added G1: NX3225GD, project_footprints:Crystal_3225, F.Cu at (195.7, 163.7)
- added G1: NX3225GD, project_footprints:Crystal_3225, F.Cu at (195.7, 129.7)
- added G1: NX3225GD, project_footprints:Crystal_3225, F.Cu at (195.7, 95.7)
- added L1: SRN3015-220M, project_footprints:BOURNS-SRN3015, F.Cu at (191.4, 170.8)
- added L1: SRN3015-220M, project_footprints:BOURNS-SRN3015, F.Cu at (191.4, 136.8)
- added L1: SRN3015-220M, project_footprints:BOURNS-SRN3015, F.Cu at (191.4, 102.8)
- added P2: CONN_01X06, project_footprints:PINHEAD1-6, F.Cu at (200.2, 151.1)
- added P2: CONN_01X06, project_footprints:PINHEAD1-6, F.Cu at (200.2, 117.1)
- added P2: CONN_01X06, project_footprints:PINHEAD1-6, F.Cu at (200.2, 83.1)
- added P3: CONN_01X05, project_footprints:PINHEAD1-5, F.Cu at (198.9, 179.0)
- added P3: CONN_01X05, project_footprints:PINHEAD1-5, F.Cu at (198.9, 145.0)
- added P3: CONN_01X05, project_footprints:PINHEAD1-5, F.Cu at (198.9, 111.0)
- added P5: CONN_01X05, project_footprints:PINHEAD1-5, F.Cu at (198.9, 153.6)
- added P5: CONN_01X05, project_footprints:PINHEAD1-5, F.Cu at (198.9, 119.6)
- added P5: CONN_01X05, project_footprints:PINHEAD1-5, F.Cu at (198.9, 85.6)
- added Q1: PSMN2R0-30YLD, project_footprints:SOT-669_LFPAK56, F.Cu at (225.0, 156.9)
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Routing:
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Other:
- board size 100 x 100 mm -> 99 x 100 mm
